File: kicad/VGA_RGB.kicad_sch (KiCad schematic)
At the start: 18 parts, among them U10 74LS157, U11 74LS04, U6 VRAM, U7 74HC245, U8 74HC244

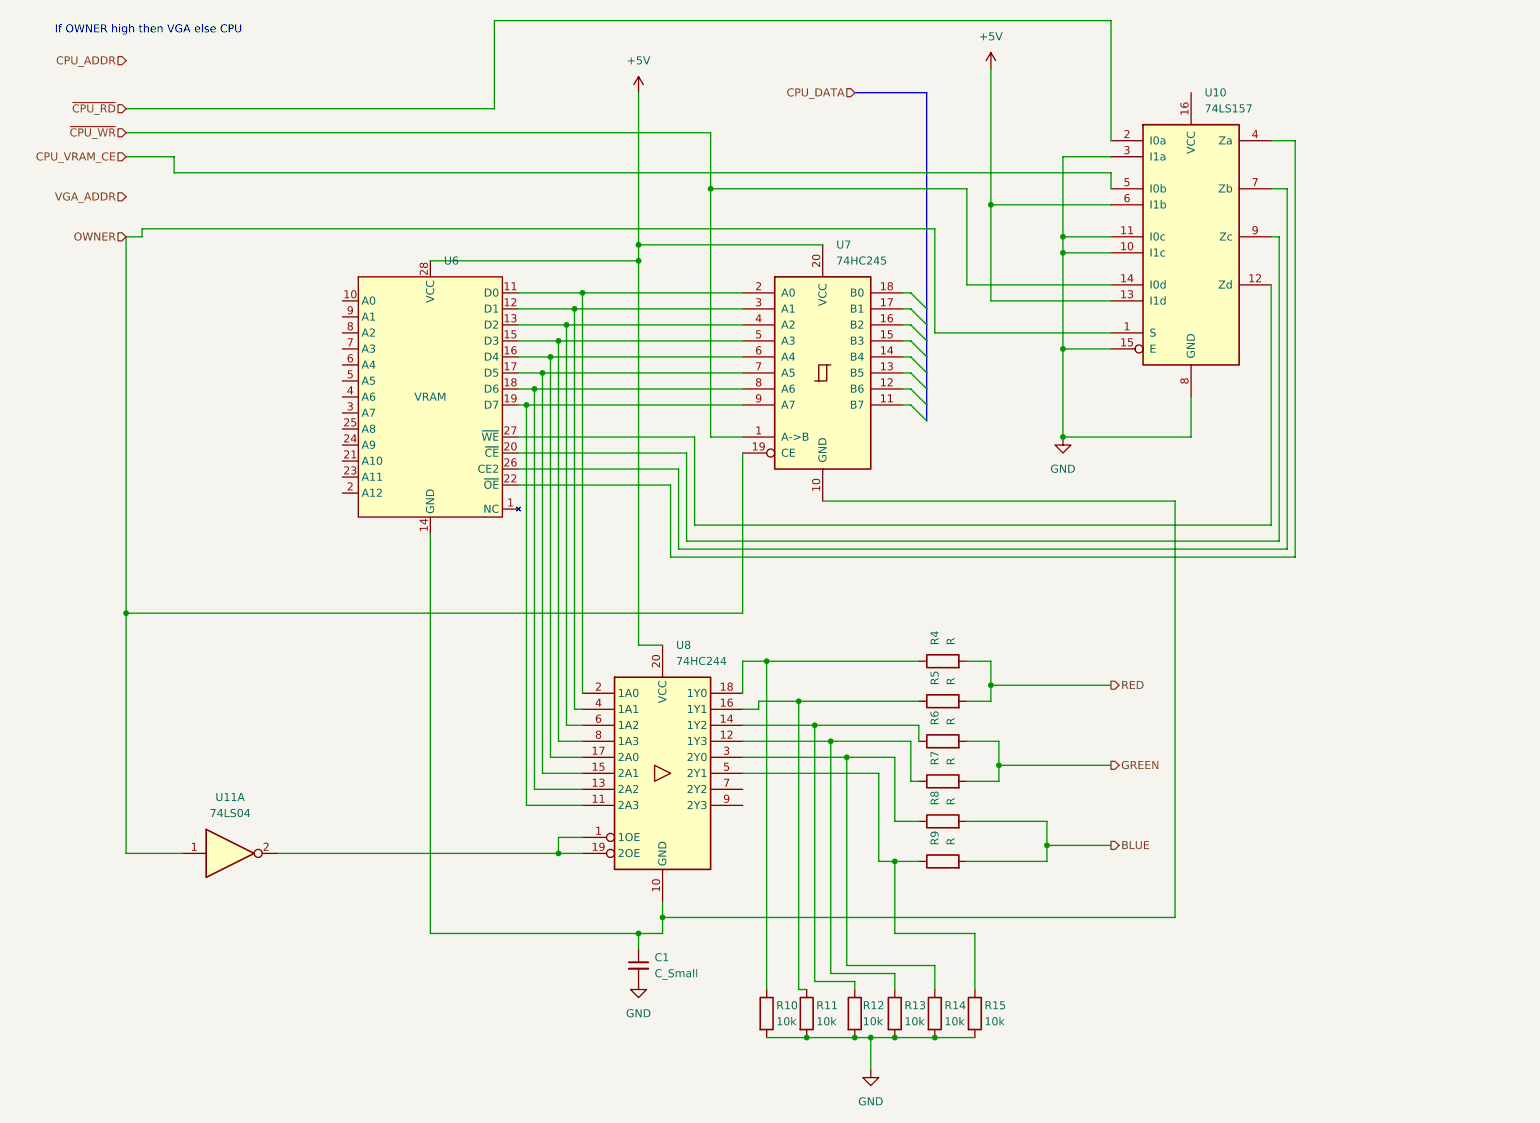
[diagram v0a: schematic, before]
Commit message: Add VRAM address multiplexer to finish off RGB schematic
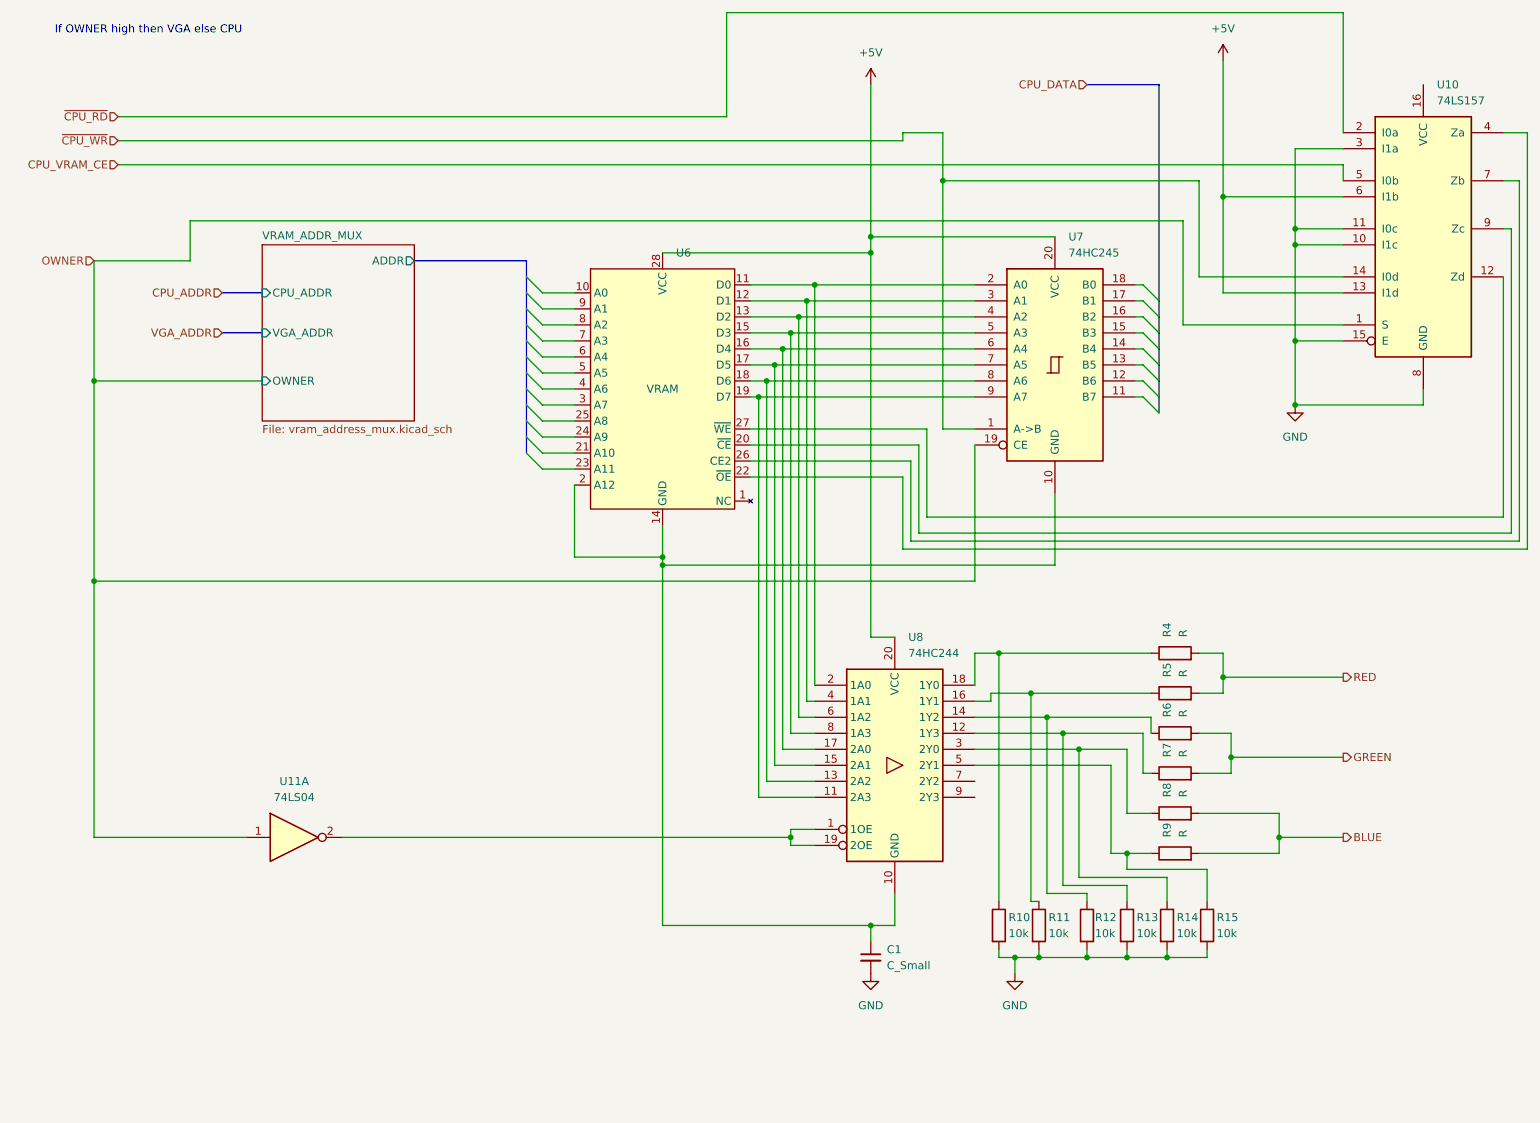
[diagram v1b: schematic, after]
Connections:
- net at C1.1, U6.14 (GND), U7.10 (GND)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: now also U6.2 (A12)
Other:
- added sheet VRAM_ADDR_MUX (vram_address_mux.kicad_sch)
- moved on the sheet: C1, R10, R11, R12, R13, R14, R15, R4, R5, R6, R7, R8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
